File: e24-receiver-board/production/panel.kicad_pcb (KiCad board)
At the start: 2 copper layers, 40 x 56.4 mm, 231 parts, among them J1 505070-2422, J10 SPEAKER-, J11 GND1, J12 TRACK_RIGHT, J13 MOTOR+, J14 U+, J15 VCC, J16 LAMP_REAR, J17 AUX2, J18 AUX4, J19 AUX11, J2 TRACK_LEFT, J20 SPEAKER+, J21 GND2, J3 MOTOR-, J4 LAMP_FRONT, J5 CAP+, J6 AUX1, J7 AUX3, J8 AUX10, J9 AUX12

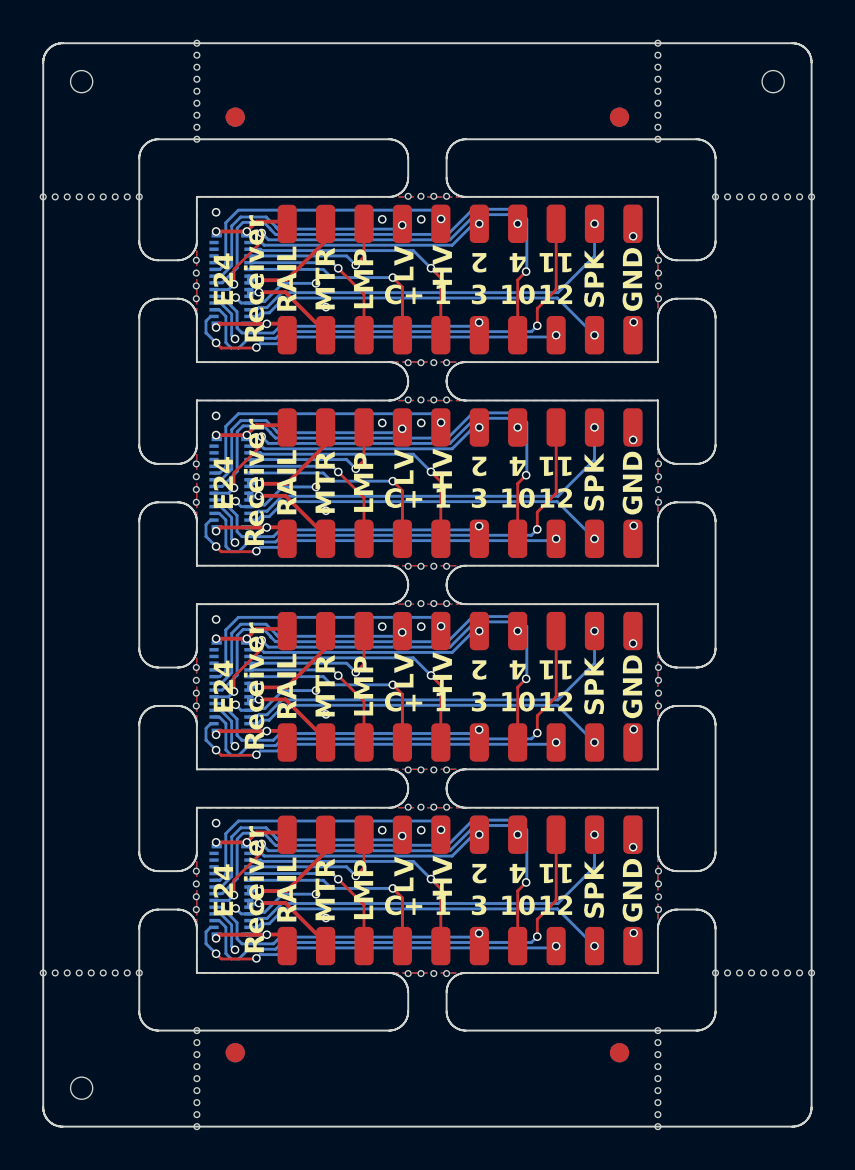
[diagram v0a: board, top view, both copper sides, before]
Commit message: fix: space out higher power terminals
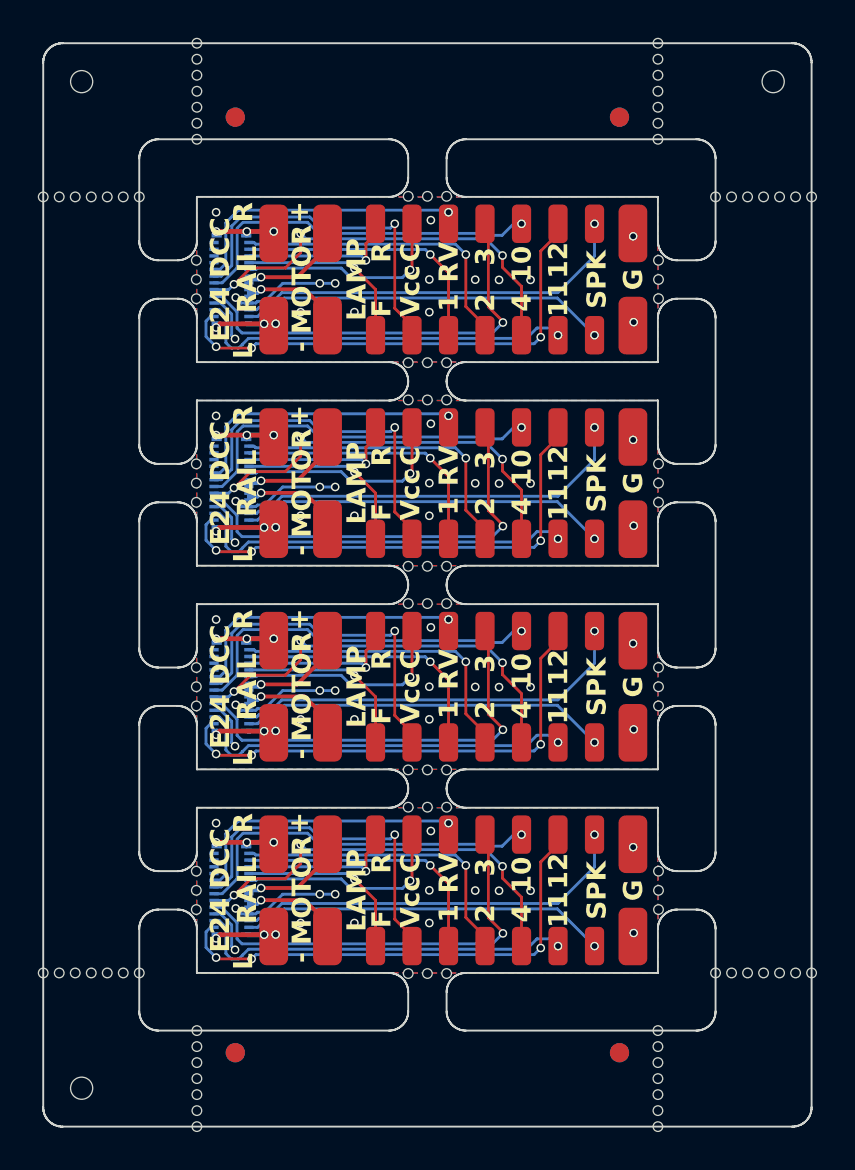
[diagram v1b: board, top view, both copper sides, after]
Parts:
- removed the J11 at (159.2, 45.8)
- removed the J11 at (159.2, 67.0)
- removed the J11 at (159.2, 35.2)
- removed the J11 at (159.2, 56.4)
- removed the J12 at (141.2, 61.2)
- removed the J12 at (141.2, 29.4)
- removed the J12 at (141.2, 50.6)
- removed the J12 at (141.2, 40.0)
- removed the J13 at (143.2, 50.6)
- removed the J13 at (143.2, 29.4)
- removed the J13 at (143.2, 40.0)
- removed the J13 at (143.2, 61.2)
- removed the J14 at (149.2, 29.4)
- removed the J14 at (149.2, 61.2)
- removed the J14 at (149.2, 50.6)
- removed the J14 at (149.2, 40.0)
- removed the J15 at (147.2, 61.2)
- removed the J15 at (147.2, 40.0)
- removed the J15 at (147.2, 29.4)
- removed the J15 at (147.2, 50.6)
- removed the J16 at (145.2, 29.4)
- removed the J16 at (145.2, 61.2)
- removed the J16 at (145.2, 40.0)
- removed the J16 at (145.2, 50.6)
- removed the J17 at (151.2, 40.0)
- removed the J17 at (151.2, 61.2)
- removed the J17 at (151.2, 29.4)
- removed the J17 at (151.2, 50.6)
- removed the J18 at (153.2, 29.4)
- removed the J18 at (153.2, 61.2)
- removed the J18 at (153.2, 50.6)
- removed the J18 at (153.2, 40.0)
- removed the J19 at (155.2, 50.6)
- removed the J19 at (155.2, 40.0)
- removed the J19 at (155.2, 61.2)
- removed the J19 at (155.2, 29.4)
- removed the J2 at (141.2, 45.8)
- removed the J2 at (141.2, 56.4)
- removed the J2 at (141.2, 67.0)
- removed the J2 at (141.2, 35.2)
- removed the J21 at (159.2, 40.0)
- removed the J21 at (159.2, 50.6)
- removed the J21 at (159.2, 61.2)
- removed the J21 at (159.2, 29.4)
- removed the J3 at (143.2, 35.2)
- removed the J3 at (143.2, 45.8)
- removed the J3 at (143.2, 67.0)
- removed the J3 at (143.2, 56.4)
- removed the J4 at (145.2, 67.0)
- removed the J4 at (145.2, 56.4)
- removed the J4 at (145.2, 45.8)
- removed the J4 at (145.2, 35.2)
- removed the J5 at (147.2, 56.4)
- removed the J5 at (147.2, 45.8)
- removed the J5 at (147.2, 67.0)
- removed the J5 at (147.2, 35.2)
- removed the J6 at (149.2, 35.2)
- removed the J6 at (149.2, 45.8)
- removed the J6 at (149.2, 56.4)
- removed the J6 at (149.2, 67.0)
- removed the J7 at (151.2, 67.0)
- removed the J7 at (151.2, 35.2)
- removed the J7 at (151.2, 56.4)
- removed the J7 at (151.2, 45.8)
- removed the J8 at (153.2, 67.0)
- removed the J8 at (153.2, 35.2)
- removed the J8 at (153.2, 45.8)
- removed the J8 at (153.2, 56.4)
- removed the J9 at (155.2, 67.0)
- removed the J9 at (155.2, 45.8)
- removed the J9 at (155.2, 35.2)
- removed the J9 at (155.2, 56.4)
- removed KiKit_MB_10_4, KiKit_MB_11_4, KiKit_MB_12_4, KiKit_MB_13_4, KiKit_MB_14_4, KiKit_MB_15_4, KiKit_MB_16_4, KiKit_MB_17_8, KiKit_MB_17_9, KiKit_MB_18_8, KiKit_MB_18_9, KiKit_MB_19_8, KiKit_MB_19_9, KiKit_MB_1_4, KiKit_MB_20_8, KiKit_MB_20_9, KiKit_MB_21_8, KiKit_MB_21_9, KiKit_MB_22_8, KiKit_MB_22_9, KiKit_MB_23_8, KiKit_MB_23_9, KiKit_MB_24_8, KiKit_MB_24_9, KiKit_MB_2_4, KiKit_MB_3_4, KiKit_MB_4_4, KiKit_MB_5_4, KiKit_MB_6_4, KiKit_MB_7_4, KiKit_MB_8_4, KiKit_MB_9_4: NPTH, NPTH
- added J11: GND1, Local Library:SolderWirePad_1x01_SMD_1.5x3mm, F.Cu at (159.2, 55.9)
- added J11: GND1, Local Library:SolderWirePad_1x01_SMD_1.5x3mm, F.Cu at (159.2, 66.5)
- added J11: GND1, Local Library:SolderWirePad_1x01_SMD_1.5x3mm, F.Cu at (159.2, 45.3)
- added J11: GND1, Local Library:SolderWirePad_1x01_SMD_1.5x3mm, F.Cu at (159.2, 34.7)
- added J12: TRACK_RIGHT, Local Library:SolderWirePad_1x01_SMD_1.5x3mm, F.Cu at (140.5, 29.9)
- added J12: TRACK_RIGHT, Local Library:SolderWirePad_1x01_SMD_1.5x3mm, F.Cu at (140.5, 40.5)
- added J12: TRACK_RIGHT, Local Library:SolderWirePad_1x01_SMD_1.5x3mm, F.Cu at (140.5, 61.7)
- added J12: TRACK_RIGHT, Local Library:SolderWirePad_1x01_SMD_1.5x3mm, F.Cu at (140.5, 51.1)
- added J13: MOTOR+, Local Library:SolderWirePad_1x01_SMD_1.5x3mm, F.Cu at (143.3, 51.1)
- added J13: MOTOR+, Local Library:SolderWirePad_1x01_SMD_1.5x3mm, F.Cu at (143.3, 29.9)
- added J13: MOTOR+, Local Library:SolderWirePad_1x01_SMD_1.5x3mm, F.Cu at (143.3, 61.7)
- added J13: MOTOR+, Local Library:SolderWirePad_1x01_SMD_1.5x3mm, F.Cu at (143.3, 40.5)
- added J14: LAMP_REAR, Connector_Wire:SolderWirePad_1x01_SMD_1x2mm, F.Cu at (145.8, 40.0)
- added J14: LAMP_REAR, Connector_Wire:SolderWirePad_1x01_SMD_1x2mm, F.Cu at (145.8, 29.4)
- added J14: LAMP_REAR, Connector_Wire:SolderWirePad_1x01_SMD_1x2mm, F.Cu at (145.8, 61.2)
- added J14: LAMP_REAR, Connector_Wire:SolderWirePad_1x01_SMD_1x2mm, F.Cu at (145.8, 50.6)
- added J15: CAP+, Connector_Wire:SolderWirePad_1x01_SMD_1x2mm, F.Cu at (147.7, 50.6)
- added J15: CAP+, Connector_Wire:SolderWirePad_1x01_SMD_1x2mm, F.Cu at (147.7, 61.2)
- added J15: CAP+, Connector_Wire:SolderWirePad_1x01_SMD_1x2mm, F.Cu at (147.7, 29.4)
- added J15: CAP+, Connector_Wire:SolderWirePad_1x01_SMD_1x2mm, F.Cu at (147.7, 40.0)
- added J16: U+, Connector_Wire:SolderWirePad_1x01_SMD_1x2mm, F.Cu at (149.6, 29.4)
- added J16: U+, Connector_Wire:SolderWirePad_1x01_SMD_1x2mm, F.Cu at (149.6, 61.2)
- added J16: U+, Connector_Wire:SolderWirePad_1x01_SMD_1x2mm, F.Cu at (149.6, 50.6)
- added J16: U+, Connector_Wire:SolderWirePad_1x01_SMD_1x2mm, F.Cu at (149.6, 40.0)
- added J17: AUX3, Connector_Wire:SolderWirePad_1x01_SMD_1x2mm, F.Cu at (151.5, 61.2)
- added J17: AUX3, Connector_Wire:SolderWirePad_1x01_SMD_1x2mm, F.Cu at (151.5, 29.4)
- added J17: AUX3, Connector_Wire:SolderWirePad_1x01_SMD_1x2mm, F.Cu at (151.5, 50.6)
- added J17: AUX3, Connector_Wire:SolderWirePad_1x01_SMD_1x2mm, F.Cu at (151.5, 40.0)
- added J18: AUX10, Connector_Wire:SolderWirePad_1x01_SMD_1x2mm, F.Cu at (153.4, 40.0)
- added J18: AUX10, Connector_Wire:SolderWirePad_1x01_SMD_1x2mm, F.Cu at (153.4, 29.4)
- added J18: AUX10, Connector_Wire:SolderWirePad_1x01_SMD_1x2mm, F.Cu at (153.4, 50.6)
- added J18: AUX10, Connector_Wire:SolderWirePad_1x01_SMD_1x2mm, F.Cu at (153.4, 61.2)
- added J19: AUX12, Connector_Wire:SolderWirePad_1x01_SMD_1x2mm, F.Cu at (155.3, 29.4)
- added J19: AUX12, Connector_Wire:SolderWirePad_1x01_SMD_1x2mm, F.Cu at (155.3, 40.0)
- added J19: AUX12, Connector_Wire:SolderWirePad_1x01_SMD_1x2mm, F.Cu at (155.3, 50.6)
- added J19: AUX12, Connector_Wire:SolderWirePad_1x01_SMD_1x2mm, F.Cu at (155.3, 61.2)
- added J2: TRACK_LEFT, Local Library:SolderWirePad_1x01_SMD_1.5x3mm, F.Cu at (140.5, 45.3)
- added J2: TRACK_LEFT, Local Library:SolderWirePad_1x01_SMD_1.5x3mm, F.Cu at (140.5, 66.5)
- added J2: TRACK_LEFT, Local Library:SolderWirePad_1x01_SMD_1.5x3mm, F.Cu at (140.5, 55.9)
- added J2: TRACK_LEFT, Local Library:SolderWirePad_1x01_SMD_1.5x3mm, F.Cu at (140.5, 34.7)
- added J21: GND2, Local Library:SolderWirePad_1x01_SMD_1.5x3mm, F.Cu at (159.2, 61.7)
- added J21: GND2, Local Library:SolderWirePad_1x01_SMD_1.5x3mm, F.Cu at (159.2, 40.5)
- added J21: GND2, Local Library:SolderWirePad_1x01_SMD_1.5x3mm, F.Cu at (159.2, 29.9)
- added J21: GND2, Local Library:SolderWirePad_1x01_SMD_1.5x3mm, F.Cu at (159.2, 51.1)
- added J3: MOTOR-, Local Library:SolderWirePad_1x01_SMD_1.5x3mm, F.Cu at (143.3, 34.7)
- added J3: MOTOR-, Local Library:SolderWirePad_1x01_SMD_1.5x3mm, F.Cu at (143.3, 66.5)
- added J3: MOTOR-, Local Library:SolderWirePad_1x01_SMD_1.5x3mm, F.Cu at (143.3, 55.9)
- added J3: MOTOR-, Local Library:SolderWirePad_1x01_SMD_1.5x3mm, F.Cu at (143.3, 45.3)
- added J4: LAMP_FRONT, Connector_Wire:SolderWirePad_1x01_SMD_1x2mm, F.Cu at (145.8, 45.8)
- added J4: LAMP_FRONT, Connector_Wire:SolderWirePad_1x01_SMD_1x2mm, F.Cu at (145.8, 35.2)
- added J4: LAMP_FRONT, Connector_Wire:SolderWirePad_1x01_SMD_1x2mm, F.Cu at (145.8, 67.0)
- added J4: LAMP_FRONT, Connector_Wire:SolderWirePad_1x01_SMD_1x2mm, F.Cu at (145.8, 56.4)
- added J5: VCC, Connector_Wire:SolderWirePad_1x01_SMD_1x2mm, F.Cu at (147.7, 56.4)
- added J5: VCC, Connector_Wire:SolderWirePad_1x01_SMD_1x2mm, F.Cu at (147.7, 35.2)
- added J5: VCC, Connector_Wire:SolderWirePad_1x01_SMD_1x2mm, F.Cu at (147.7, 67.0)
- added J5: VCC, Connector_Wire:SolderWirePad_1x01_SMD_1x2mm, F.Cu at (147.7, 45.8)
- added J6: AUX1, Connector_Wire:SolderWirePad_1x01_SMD_1x2mm, F.Cu at (149.6, 45.8)
- added J6: AUX1, Connector_Wire:SolderWirePad_1x01_SMD_1x2mm, F.Cu at (149.6, 67.0)
- added J6: AUX1, Connector_Wire:SolderWirePad_1x01_SMD_1x2mm, F.Cu at (149.6, 56.4)
- added J6: AUX1, Connector_Wire:SolderWirePad_1x01_SMD_1x2mm, F.Cu at (149.6, 35.2)
- added J7: AUX2, Connector_Wire:SolderWirePad_1x01_SMD_1x2mm, F.Cu at (151.5, 67.0)
- added J7: AUX2, Connector_Wire:SolderWirePad_1x01_SMD_1x2mm, F.Cu at (151.5, 56.4)
- added J7: AUX2, Connector_Wire:SolderWirePad_1x01_SMD_1x2mm, F.Cu at (151.5, 45.8)
- added J7: AUX2, Connector_Wire:SolderWirePad_1x01_SMD_1x2mm, F.Cu at (151.5, 35.2)
- added J8: AUX4, Connector_Wire:SolderWirePad_1x01_SMD_1x2mm, F.Cu at (153.4, 67.0)
- added J8: AUX4, Connector_Wire:SolderWirePad_1x01_SMD_1x2mm, F.Cu at (153.4, 35.2)
- added J8: AUX4, Connector_Wire:SolderWirePad_1x01_SMD_1x2mm, F.Cu at (153.4, 56.4)
- added J8: AUX4, Connector_Wire:SolderWirePad_1x01_SMD_1x2mm, F.Cu at (153.4, 45.8)
- added J9: AUX11, Connector_Wire:SolderWirePad_1x01_SMD_1x2mm, F.Cu at (155.3, 45.8)
- added J9: AUX11, Connector_Wire:SolderWirePad_1x01_SMD_1x2mm, F.Cu at (155.3, 56.4)
- added J9: AUX11, Connector_Wire:SolderWirePad_1x01_SMD_1x2mm, F.Cu at (155.3, 35.2)
- added J9: AUX11, Connector_Wire:SolderWirePad_1x01_SMD_1x2mm, F.Cu at (155.3, 67.0)
- moved KiKit_MB_17_7 1.25 mm to (136.5, 25.0)
- moved KiKit_MB_18_7 1.25 mm to (160.5, 25.0)
- moved KiKit_MB_19_7 1.25 mm to (136.5, 76.4)
- moved KiKit_MB_20_7 1.25 mm to (160.5, 76.4)
- moved KiKit_MB_21_7 1.25 mm to (133.5, 28.0)
- moved KiKit_MB_22_7 1.25 mm to (133.5, 68.4)
- moved KiKit_MB_23_7 1.25 mm to (168.5, 28.0)
- moved KiKit_MB_24_7 1.25 mm to (168.5, 68.4)
- moved KiKit_MB_17_6 1.04 mm to (136.5, 24.2)
- moved KiKit_MB_18_6 1.04 mm to (160.5, 24.2)
- moved KiKit_MB_21_6 1.04 mm to (132.7, 28.0)
- moved KiKit_MB_22_6 1.04 mm to (132.7, 68.4)
- moved KiKit_MB_19_6 1.04 mm to (136.5, 75.6)
- moved KiKit_MB_20_6 1.04 mm to (160.5, 75.6)
- moved KiKit_MB_23_6 1.04 mm to (167.7, 28.0)
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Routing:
- net Board_3-/AUX10: track 26.1 -> 19.2 mm
- net Board_1-/AUX10: track 26.1 -> 19.2 mm
- net Board_0-/AUX10: track 26.1 -> 19.2 mm
- net Board_2-/AUX10: track 26.1 -> 19.2 mm
- net Board_3-/AUX3: track 15.3 -> 21.8 mm
- net Board_1-/AUX3: track 15.3 -> 21.8 mm
- net Board_2-/AUX3: track 15.3 -> 21.8 mm
- net Board_0-/AUX3: track 15.3 -> 21.8 mm
- net Board_2-VCC: track 12.6 -> 18.4 mm
- net Board_1-VCC: track 12.6 -> 18.4 mm
- net Board_0-VCC: track 12.6 -> 18.4 mm
- net Board_3-VCC: track 12.6 -> 18.4 mm
- net Board_0-/AUX12: track 20.0 -> 25.5 mm
- net Board_3-/AUX12: track 20.0 -> 25.5 mm
- net Board_2-/AUX12: track 20.0 -> 25.5 mm
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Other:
- board text added: "+"
- board text added: "-"
- board text added: "C"
- board text added: "E24 Adapter"
- board text added: "E24 DCC"
- board text added: "F"
- board text added: "G"
- board text added: "L"
- board text added: "LAMP"
- board text added: "MOTOR"
- board text added: "R"
- board text added: "RV"
- board text added: "Vcc"
- board text removed: "C+"
- board text removed: "E24 Receiver"
- board text removed: "GND"
- board text removed: "HV"
- board text removed: "LMP"
- board text removed: "LV"
- board text removed: "MTR"
